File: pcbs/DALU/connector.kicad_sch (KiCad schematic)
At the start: 6 parts, among them J201 Conn_02x20_Odd_Even, U201 74HC245, U202 74HC245, U203 74HC245

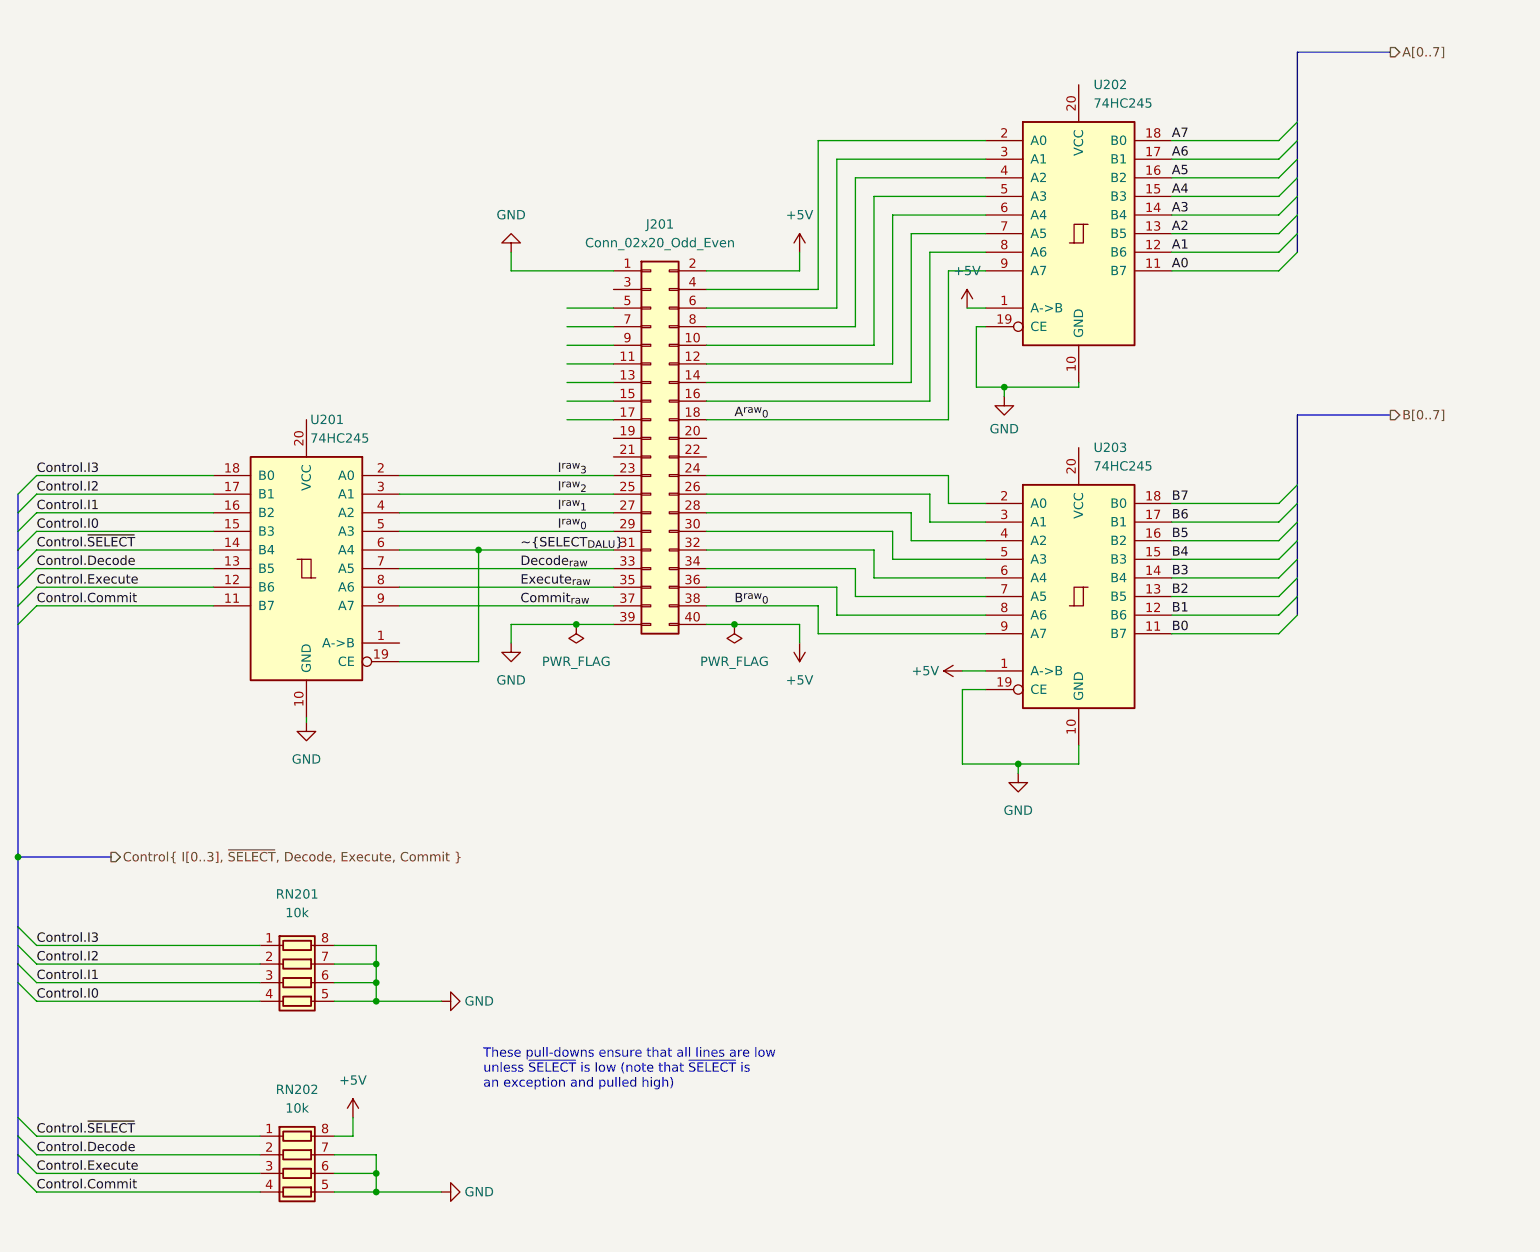
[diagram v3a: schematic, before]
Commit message: Rerouting
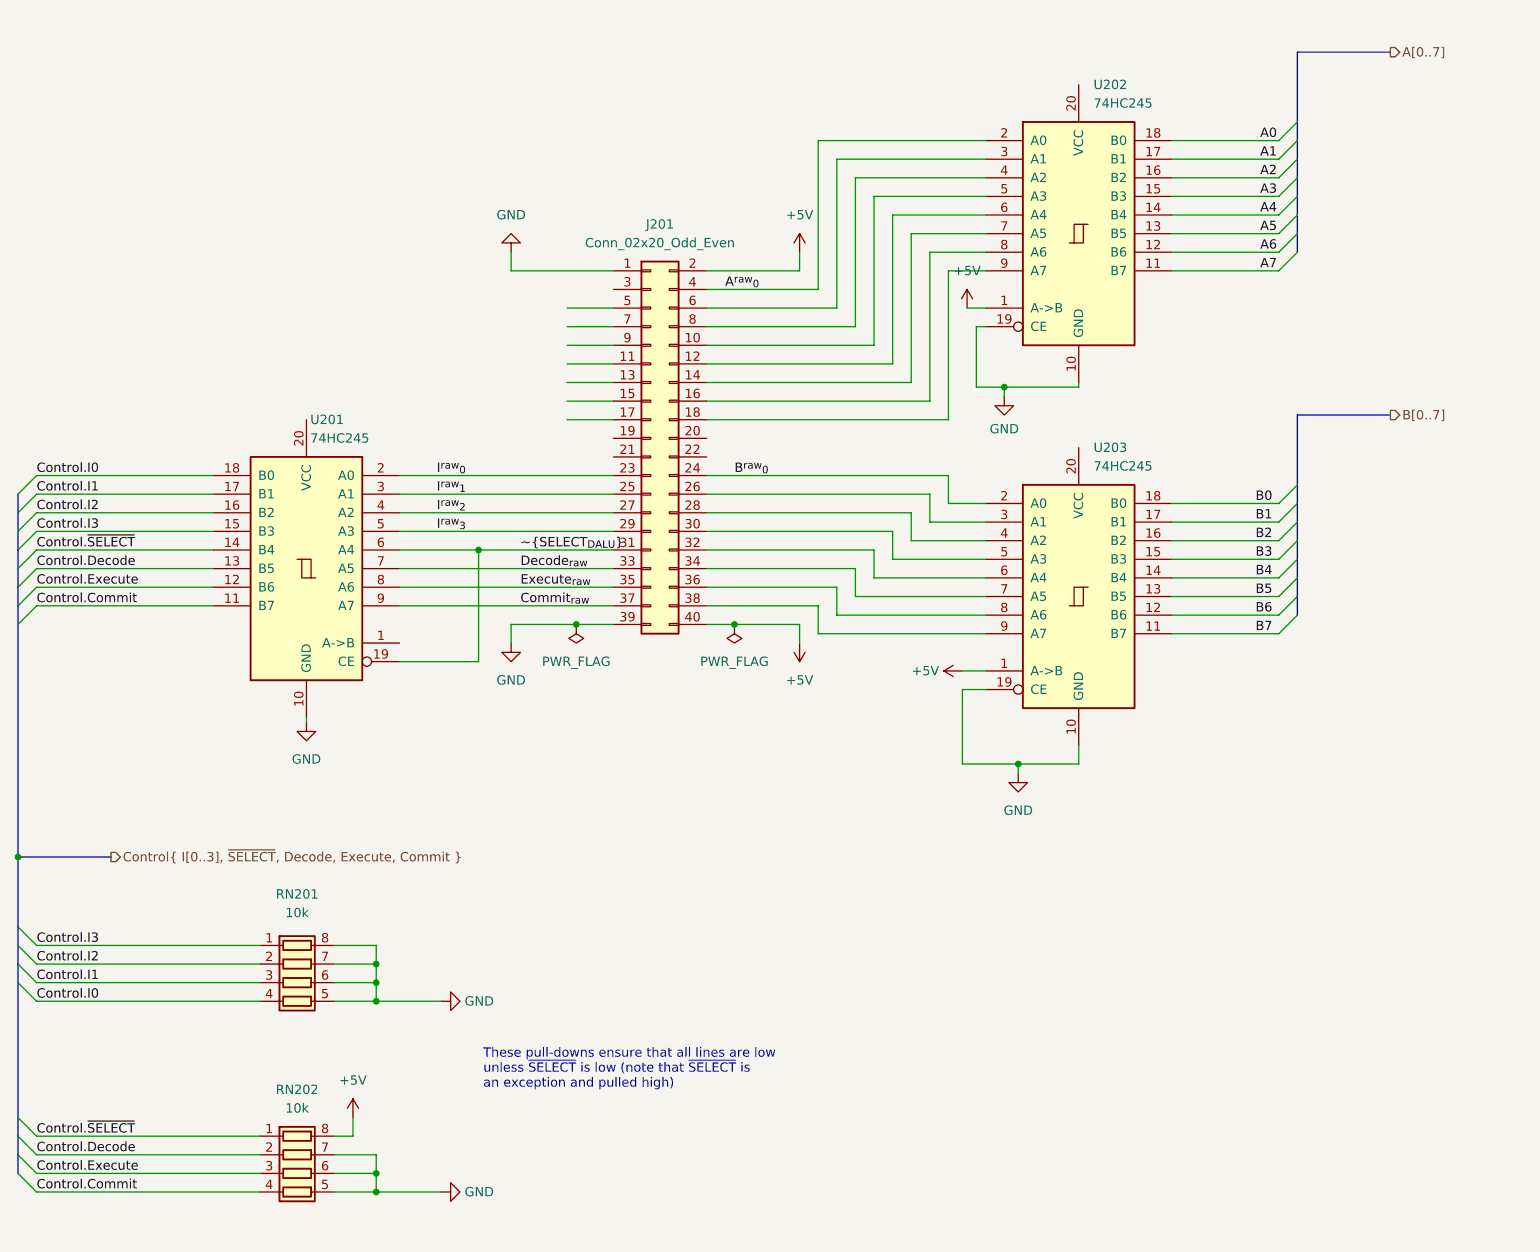
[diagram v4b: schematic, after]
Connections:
- net A0: now also U202.18 (B0); no longer U202.11 (B7)
- net A1: now also U202.17 (B1); no longer U202.12 (B6)
- net A2: now also U202.16 (B2); no longer U202.13 (B5)
- net A3: now also U202.15 (B3); no longer U202.14 (B4)
- net A4: now also U202.14 (B4); no longer U202.15 (B3)
- net A5: now also U202.13 (B5); no longer U202.16 (B2)
- net A6: now also U202.12 (B6); no longer U202.17 (B1)
- net A7: now also U202.11 (B7); no longer U202.18 (B0)
- net A^{raw}_{0}: now also J201.4 (Pin_4), U202.2 (A0); no longer J201.18 (Pin_18), U202.9 (A7)
- net B0: now also U203.18 (B0); no longer U203.11 (B7)
- net B1: now also U203.17 (B1); no longer U203.12 (B6)
- net B2: now also U203.16 (B2); no longer U203.13 (B5)
- net B3: now also U203.15 (B3); no longer U203.14 (B4)
- net B4: now also U203.14 (B4); no longer U203.15 (B3)
- net B5: now also U203.13 (B5); no longer U203.16 (B2)
- net B6: now also U203.12 (B6); no longer U203.17 (B1)
- net B7: now also U203.11 (B7); no longer U203.18 (B0)
- net B^{raw}_{0}: now also J201.24 (Pin_24), U203.2 (A0); no longer J201.38 (Pin_38), U203.9 (A7)
- net Control.I0: now also U201.18 (B0); no longer U201.15 (B3)
- net Control.I1: now also U201.17 (B1); no longer U201.16 (B2)
- net Control.I2: now also U201.16 (B2); no longer U201.17 (B1)
- net Control.I3: now also U201.15 (B3); no longer U201.18 (B0)
- net I^{raw}_{0}: now also J201.23 (Pin_23), U201.2 (A0); no longer J201.29 (Pin_29), U201.5 (A3)
- net I^{raw}_{1}: now also J201.25 (Pin_25), U201.3 (A1); no longer J201.27 (Pin_27), U201.4 (A2)
- net I^{raw}_{2}: now also J201.27 (Pin_27), U201.4 (A2); no longer J201.25 (Pin_25), U201.3 (A1)
- net I^{raw}_{3}: now also J201.29 (Pin_29), U201.5 (A3); no longer J201.23 (Pin_23), U201.2 (A0)
- new net: J201.38 (Pin_38), U203.9 (A7)
- new net: J201.18 (Pin_18), U202.9 (A7)
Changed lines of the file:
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@@
     (effects (font (size 1.27 1.27)) (justify left bottom))
   )
-  (label "B0" (at 176.53 114.3 0)
+  (label "B0" (at 187.96 96.52 0)
     (effects (font (size 1.27 1.27)) (justify left bottom))
   )
-  (label "A3" (at 176.53 57.15 0)
+  (label "A3" (at 188.595 54.61 0)
     (effects (font (size 1.27 1.27)) (justify left bottom))
   )
-  (label "Control.I1" (at 21.59 97.79 0)
+  (label "Control.I1" (at 21.59 95.25 0)
     (effects (font (size 1.27 1.27)) (justify left bottom))
   )
-  (label "B4" (at 176.53 104.14 0)
+  (label "B4" (at 187.96 106.68 0)
     (effects (font (size 1.27 1.27)) (justify left bottom))
   )
@@
     (effects (font (size 1.27 1.27)) (justify left bottom))
   )
-  (label "Control.I0" (at 21.59 100.33 0)
+  (label "Control.I0" (at 21.59 92.71 0)
     (effects (font (size 1.27 1.27)) (justify left bottom))
   )
-  (label "A0" (at 176.53 64.77 0)
+  (label "A0" (at 188.595 46.99 0)
     (effects (font (size 1.27 1.27)) (justify left bottom))
   )
@@
     (effects (font (size 1.27 1.27)) (justify left bottom))
   )
-  (label "B^{raw}_{0}" (at 116.84 110.49 0)
+  (label "B^{raw}_{0}" (at 116.84 92.71 0)
     (effects (font (size 1.27 1.27)) (justify left bottom))
   )
-  (label "Control.I2" (at 21.59 95.25 0)
+  (label "Control.I2" (at 21.59 97.79 0)
     (effects (font (size 1.27 1.27)) (justify left bottom))
   )
-  (label "B7" (at 176.53 96.52 0)
+  (label "B7" (at 187.96 114.3 0)
     (effects (font (size 1.27 1.27)) (justify left bottom))
   )
@@
     (effects (font (size 1.27 1.27)) (justify left bottom))
   )
-  (label "A4" (at 176.53 54.61 0)
+  (label "A4" (at 188.595 57.15 0)
     (effects (font (size 1.27 1.27)) (justify left bottom))
   )
@@
     (effects (font (size 1.27 1.27)) (justify left bottom))
   )
-  (label "I^{raw}_{3}" (at 92.71 92.71 0)
+  (label "I^{raw}_{3}" (at 76.2 100.33 0)
     (effects (font (size 1.27 1.27)) (justify left bottom))
   )
-  (label "B6" (at 176.53 99.06 0)
+  (label "B6" (at 187.96 111.76 0)
     (effects (font (size 1.27 1.27)) (justify left bottom))
   )
@@
     (effects (font (size 1.27 1.27)) (justify left bottom))
   )
-  (label "A5" (at 176.53 52.07 0)
+  (label "A5" (at 188.595 59.69 0)
     (effects (font (size 1.27 1.27)) (justify left bottom))
   )
-  (label "B2" (at 176.53 109.22 0)
+  (label "B2" (at 187.96 101.6 0)
     (effects (font (size 1.27 1.27)) (justify left bottom))
   )
@@
     (effects (font (size 1.27 1.27)) (justify left bottom))
   )
-  (label "A6" (at 176.53 49.53 0)
+  (label "A6" (at 188.595 62.23 0)
     (effects (font (size 1.27 1.27)) (justify left bottom))
   )
-  (label "B1" (at 176.53 111.76 0)
+  (label "B1" (at 187.96 99.06 0)
     (effects (font (size 1.27 1.27)) (justify left bottom))
   )
-  (label "A7" (at 176.53 46.99 0)
+  (label "A7" (at 188.595 64.77 0)
     (effects (font (size 1.27 1.27)) (justify left bottom))
   )
-  (label "B5" (at 176.53 101.6 0)
+  (label "B5" (at 187.96 109.22 0)
     (effects (font (size 1.27 1.27)) (justify left bottom))
   )
@@
     (effects (font (size 1.27 1.27)) (justify left bottom))
   )
-  (label "Control.I3" (at 21.59 92.71 0)
+  (label "Control.I3" (at 21.59 100.33 0)
     (effects (font (size 1.27 1.27)) (justify left bottom))
   )
-  (label "B3" (at 176.53 106.68 0)
+  (label "B3" (at 187.96 104.14 0)
     (effects (font (size 1.27 1.27)) (justify left bottom))
   )
-  (label "I^{raw}_{2}" (at 92.71 95.25 0)
+  (label "I^{raw}_{2}" (at 76.2 97.79 0)
     (effects (font (size 1.27 1.27)) (justify left bottom))
   )
@@
     (effects (font (size 1.27 1.27)) (justify left bottom))
   )
-  (label "A^{raw}_{0}" (at 116.84 85.09 0)
+  (label "A^{raw}_{0}" (at 115.57 67.31 0)
     (effects (font (size 1.27 1.27)) (justify left bottom))
   )
-  (label "I^{raw}_{0}" (at 92.71 100.33 0)
+  (label "I^{raw}_{0}" (at 76.2 92.71 0)
     (effects (font (size 1.27 1.27)) (justify left bottom))
   )
@@
     (effects (font (size 1.27 1.27)) (justify left bottom))
   )
-  (label "A2" (at 176.53 59.69 0)
+  (label "A2" (at 188.595 52.07 0)
     (effects (font (size 1.27 1.27)) (justify left bottom))
   )
-  (label "A1" (at 176.53 62.23 0)
+  (label "A1" (at 188.595 49.53 0)
     (effects (font (size 1.27 1.27)) (justify left bottom))
   )
@@
     (effects (font (size 1.27 1.27)) (justify left bottom))
   )
-  (label "I^{raw}_{1}" (at 92.71 97.79 0)
+  (label "I^{raw}_{1}" (at 76.2 95.25 0)
     (effects (font (size 1.27 1.27)) (justify left bottom))
   )

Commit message: Redoing resistors
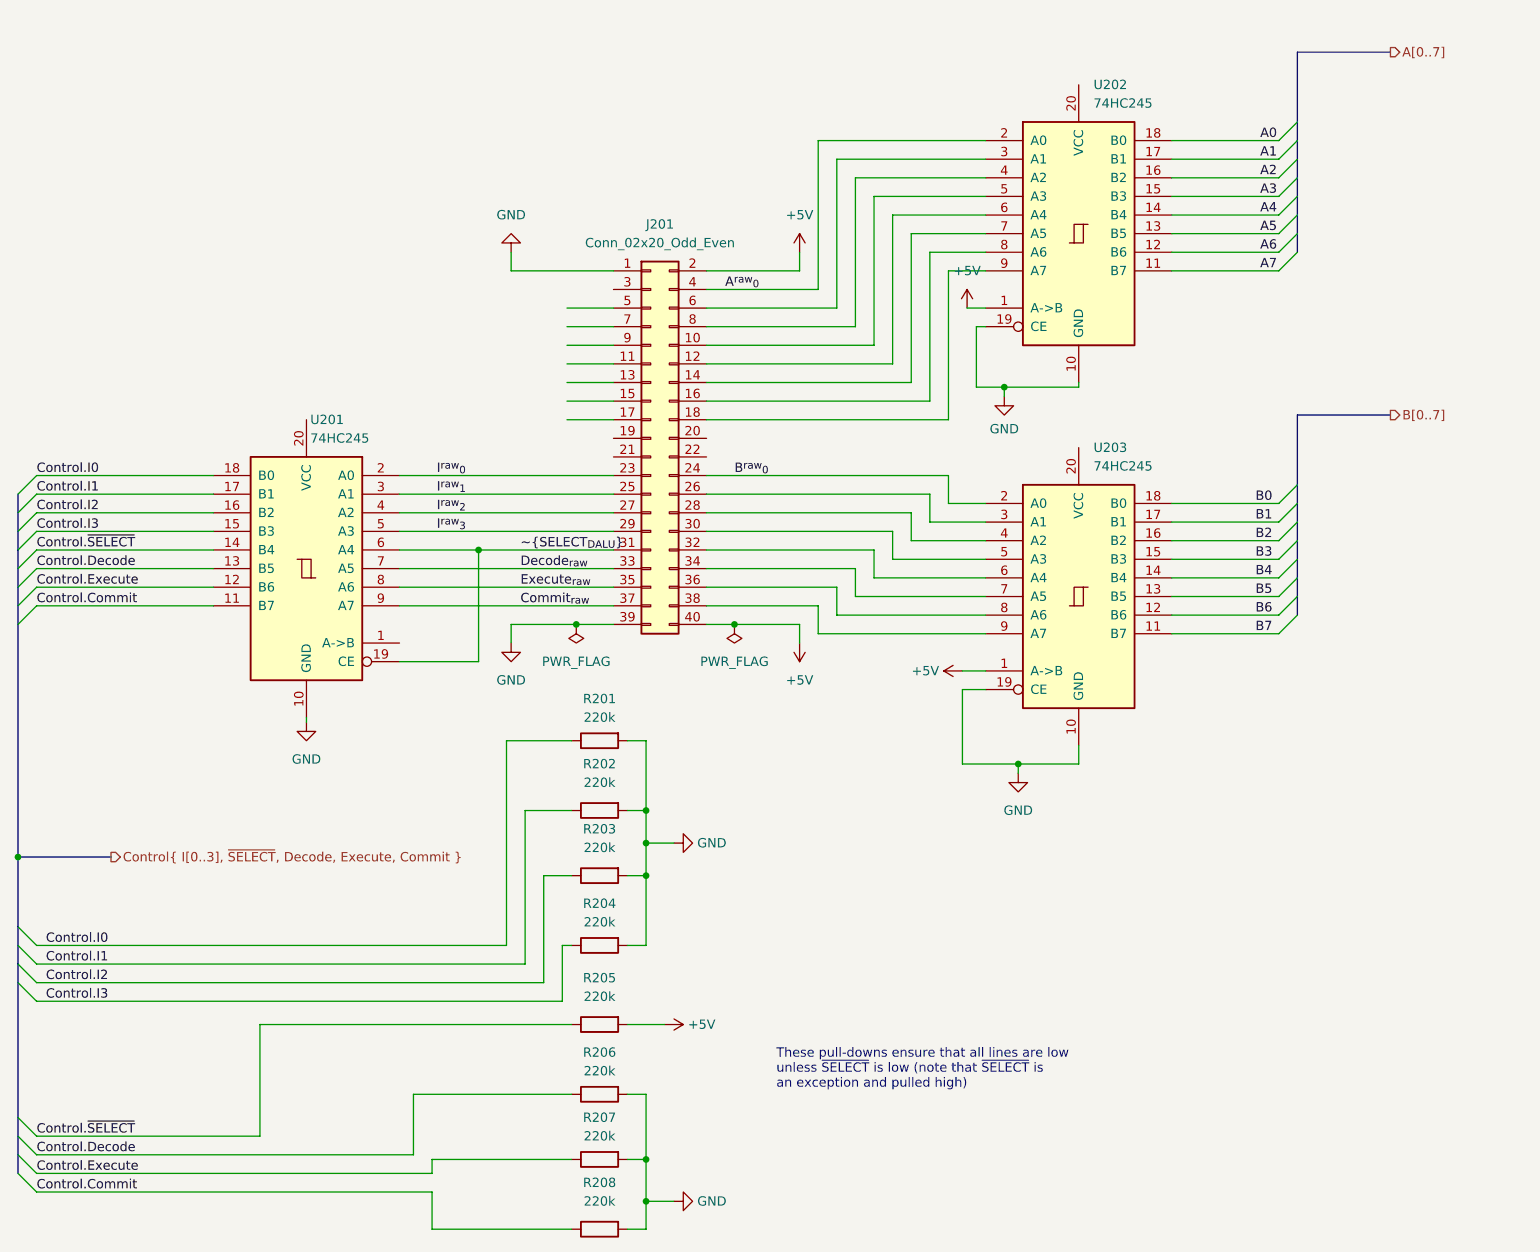
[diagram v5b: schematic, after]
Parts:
- removed RN201, RN202: 10k, Resistor_SMD:R_Array_Convex_4x0402, symbol Device:R_Pack04
- added R201, R202, R203, R204, R205, R206, R207, R208: 220k, Resistor_SMD:R_0603_1608Metric, symbol Device:R
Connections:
- net +5V: now also R205.2
- net Control.Commit: now also R208.1
- net Control.Decode: now also R206.1
- net Control.Execute: now also R207.1
- net Control.I0: now also R201.1
- net Control.I1: now also R202.1
- net Control.I2: now also R203.1
- net Control.I3: now also R204.1
- net Control.~{SELECT}: now also R205.1
- net GND: now also R201.2, R202.2, R203.2, R204.2, R206.2, R207.2, R208.2

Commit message: Finish preliminary routing
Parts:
- added C201, C202, C203: 100n, Capacitor_SMD:C_0603_1608Metric, symbol Device:C
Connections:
- net +5V: now also U201.1 (A->B), U201.20 (VCC), U202.20 (VCC), U203.20 (VCC), C201.1, C202.1, C203.1
- net GND: now also C201.2, C202.2, C203.2
- net C4: now reaches J201.11 (Pin_11)
- net C5: now reaches J201.13 (Pin_13)
- net C6: now reaches J201.15 (Pin_15)
- net C7: now reaches J201.17 (Pin_17)
- net DALUFLAG: now reaches J201.19 (Pin_19)
- net C0: now reaches J201.3 (Pin_3)
- net C1: now reaches J201.5 (Pin_5)
- net C2: now reaches J201.7 (Pin_7)
- net C3: now reaches J201.9 (Pin_9)

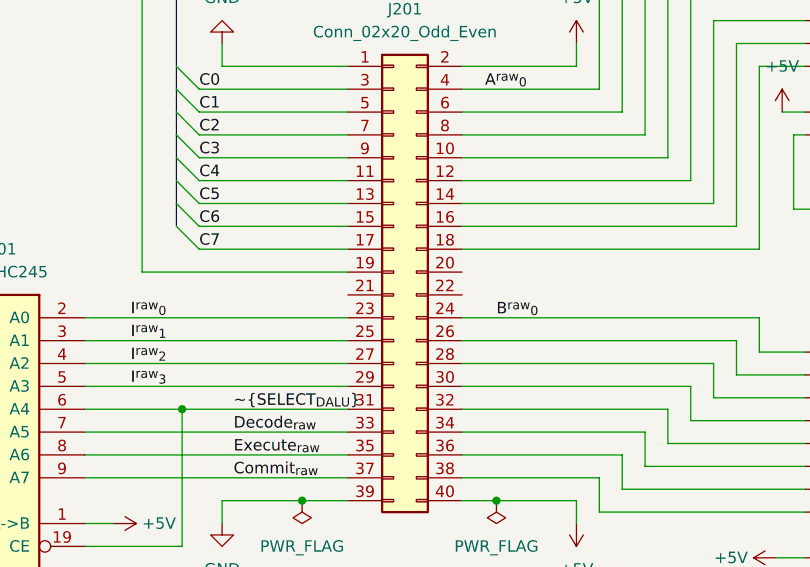
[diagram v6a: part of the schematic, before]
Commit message: Filling out connections
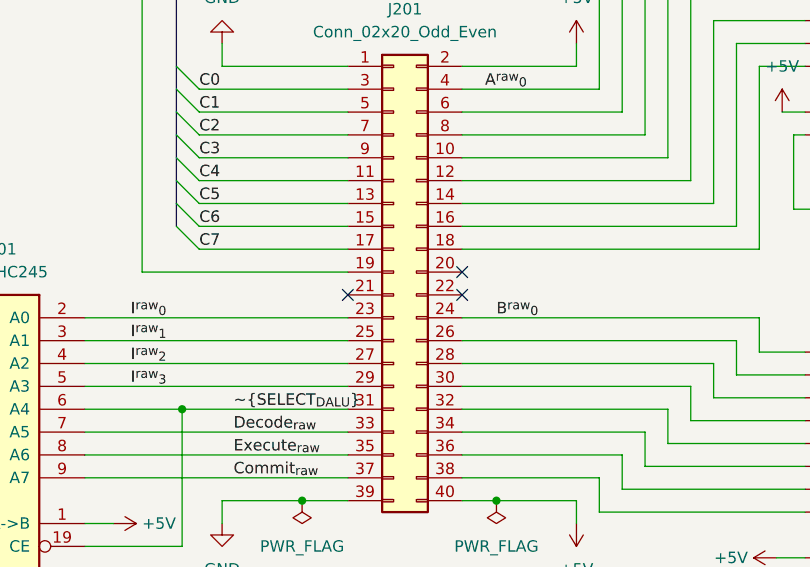
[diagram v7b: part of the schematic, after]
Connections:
- no-connect marks 0 -> 3
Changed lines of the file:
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@@
   (junction (at 155.575 132.08) (diameter 0) (color 0 0 0 0)
   )
+  (no_connect (at 100.33 90.17))
+  (no_connect (at 113.03 90.17))
+  (no_connect (at 113.03 87.63))
   (bus_entry (at 81.28 72.39) (size 2.54 2.54)
     (stroke (width 0) (type default) (color 0 0 0 0))
